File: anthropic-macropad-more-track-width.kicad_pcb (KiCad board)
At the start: 2 copper layers, 136 x 81 mm, 14 parts, among them SW1 ESC, SW10 ENTER, SW11 MIC, SW2 TAB, SW3 ALLOW_ONCE, SW4 UP, SW5 ALLOW_ALWAYS, SW6 LEFT, SW7 DOWN, SW8 RIGHT, SW9 REJECT, U1 XIAO_RP2040

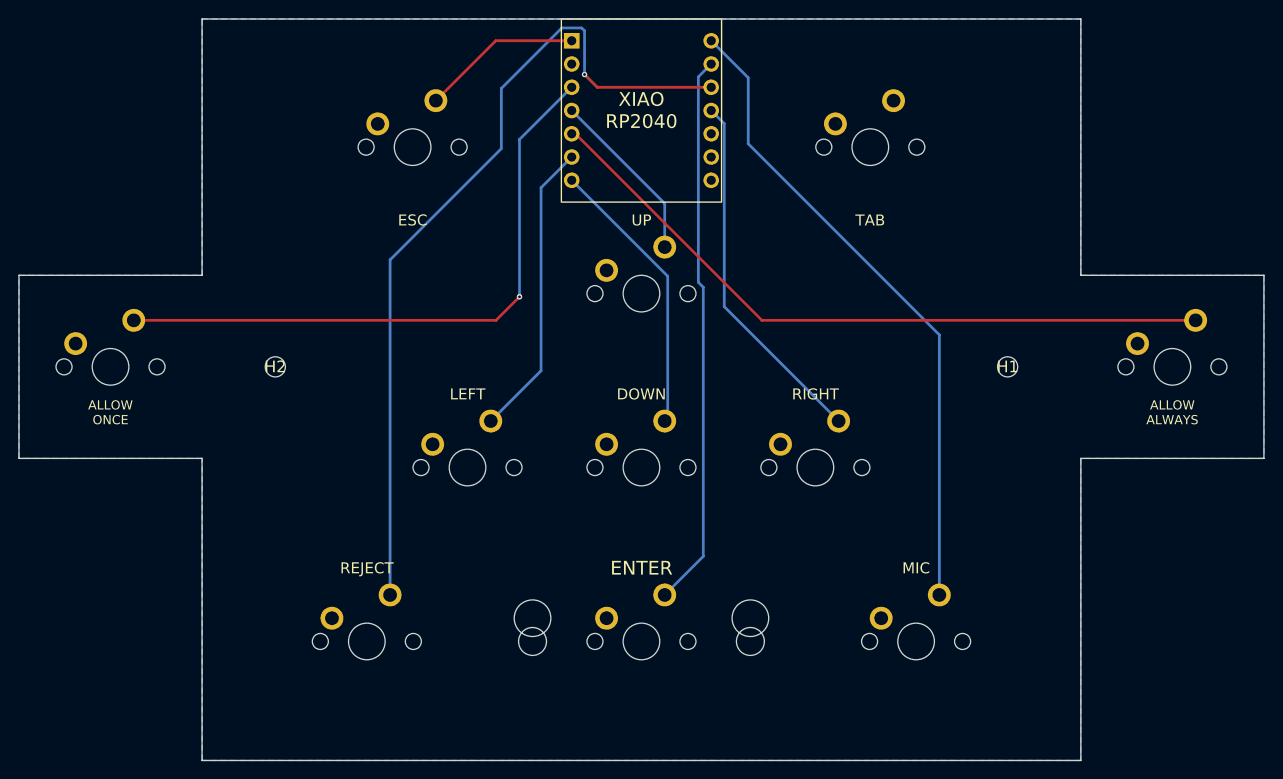
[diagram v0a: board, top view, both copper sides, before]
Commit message: Replace 2 mounting holes with 4 corner mounting holes
Co-Authored-By: Claude Opus 4.6 <noreply@anthropic.com>
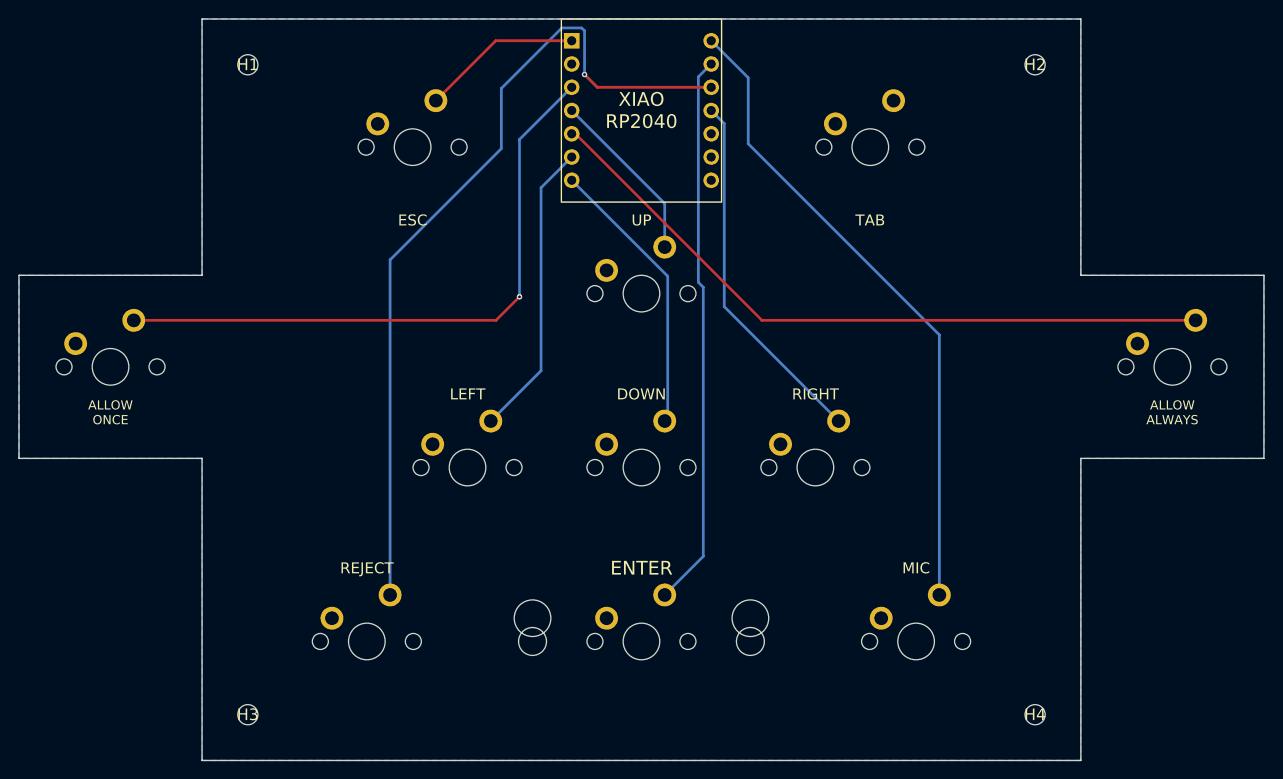
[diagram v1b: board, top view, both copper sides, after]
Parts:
- added H3: , MountingHole:MountingHole_2.2mm_M2, F.Cu at (57.0, 106.0)
- added H4: , MountingHole:MountingHole_2.2mm_M2, F.Cu at (143.0, 106.0)
- moved H1 89.3 mm to (57.0, 35.0)
- moved H2 89.3 mm to (143.0, 35.0)
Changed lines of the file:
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@@
 	(footprint "MountingHole:MountingHole_2.2mm_M2"
 		(layer "F.Cu")
-		(at 140 68)
+		(at 57 35)
 		(descr "Mounting Hole 2.2mm M2")
 		(property "Reference" "H1"
@@
 		(embedded_fonts no)
 	)
+	(footprint "MountingHole:MountingHole_2.2mm_M2"
+		(layer "F.Cu")
+		(at 143 106)
+		(descr "Mounting Hole 2.2mm M2")
+		(property "Reference" "H4"
+			(at 0 0 0)
+			(layer "F.SilkS")
+			(effects
+				(font
+					(size 1.27 1.27)
+				)
+			)
+		)
+		(property "Value" ""
+			(at 0 0 0)
+			(layer "F.Fab")
+			(effects
+				(font
+					(size 1.27 1.27)
+				)
+			)
+		)
+		(property "Datasheet" ""
+			(at 0 0 0)
+			(layer "F.Fab")
+			(hide yes)
+			(effects
+				(font
+					(size 1.27 1.27)
+				)
+			)
+		)
+		(property "Description" ""
+			(at 0 0 0)
+			(layer "F.Fab")
+			(hide yes)
+			(effects
+				(font
+					(size 1.27 1.27)
+				)
+			)
+		)
+		(attr exclude_from_pos_files exclude_from_bom)
+		(duplicate_pad_numbers_are_jumpers no)
+		(pad "" np_thru_hole circle
+			(at 0 0)
+			(size 2.2 2.2)
+			(drill 2.2)
+			(layers "*.Cu" "*.Mask")
+		)
+		(embedded_fonts no)
+	)
 	(footprint "Switch:SW_Cherry_MX_1u"
 		(layer "F.Cu")
@@
 	(footprint "MountingHole:MountingHole_2.2mm_M2"
 		(layer "F.Cu")
-		(at 60 68)
+		(at 143 35)
 		(descr "Mounting Hole 2.2mm M2")
 		(property "Reference" "H2"
@@
 		)
 		(embedded_fonts no)
+	)
+	(footprint "MountingHole:MountingHole_2.2mm_M2"
+		(layer "F.Cu")
+		(at 57 106)
+		(descr "Mounting Hole 2.2mm M2")
+		(property "Reference" "H3"
+			(at 0 0 0)
+			(layer "F.SilkS")
+			(effects
+				(font
+					(size 1.27 1.27)
+				)
+			)
+		)
+		(property "Value" ""
+			(at 0 0 0)
+			(layer "F.Fab")
+			(effects
+				(font
+					(size 1.27 1.27)
+				)
+			)
+		)
+		(property "Datasheet" ""
+			(at 0 0 0)
+			(layer "F.Fab")
+			(hide yes)
+			(effects
+				(font
+					(size 1.27 1.27)
+				)
+			)
+		)
+		(property "Description" ""
+			(at 0 0 0)
+			(layer "F.Fab")
+			(hide yes)
+			(effects
+				(font
+					(size 1.27 1.27)
+				)
+			)
+		)
+		(attr exclude_from_pos_files exclude_from_bom)
+		(duplicate_pad_numbers_are_jumpers no)
+		(pad "" np_thru_hole circle
+			(at 0 0)
+			(size 2.2 2.2)
+			(drill 2.2)
+			(layers "*.Cu" "*.Mask")
+		)
+		(embedded_fonts no)

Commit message: Fix GND pour connection and SW_TAB trace, DRC clean
Co-Authored-By: Claude Opus 4.6 <noreply@anthropic.com>
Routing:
- net SW_TAB: track 0.00 -> 67.9 mm
- net SW_ENTER: track 60.6 -> 85.5 mm
- net SW_MIC: track 70.9 -> 81.6 mm
- net SW_REJECT: track 91.5 -> 87.3 mm, vias 1 -> 0
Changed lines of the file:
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@@
 	)
 	(segment
-		(start 109.0415 41.4215)
+		(start 121.54 73.92)
+		(end 121.54 67.04)
+		(width 0.3)
+		(layer "B.Cu")
+		(net "SW_RIGHT")
+	)
+	(segment
+		(start 112 57.5)
+		(end 112 44.38)
+		(width 0.3)
+		(layer "B.Cu")
+		(net "SW_RIGHT")
+	)
+	(segment
+		(start 112 44.38)
 		(end 107.62 40)
 		(width 0.3)
@@
 	)
 	(segment
-		(start 109.0415 61.4215)
-		(end 109.0415 41.4215)
+		(start 121.54 67.04)
+		(end 112 57.5)
 		(width 0.3)
 		(layer "B.Cu")
@@
 	)
 	(segment
-		(start 121.54 73.92)
-		(end 109.0415 61.4215)
-		(width 0.3)
-		(layer "B.Cu")
-		(net "SW_RIGHT")
+		(start 92.38 34.92)
+		(end 102.5 45.04)
+		(width 0.3)
+		(layer "F.Cu")
+		(net "SW_TAB")
+	)
+	(segment
+		(start 102.5 48.5)
+		(end 108.5 54.5)
+		(width 0.3)
+		(layer "F.Cu")
+		(net "SW_TAB")
+	)
+	(segment
+		(start 129.42 38.92)
+		(end 127.54 38.92)
+		(width 0.3)
+		(layer "F.Cu")
+		(net "SW_TAB")
+	)
+	(segment
+		(start 108.5 54.5)
+		(end 128.5 54.5)
+		(width 0.3)
+		(layer "F.Cu")
+		(net "SW_TAB")
+	)
+	(segment
+		(start 128.5 54.5)
+		(end 134 49)
+		(width 0.3)
+		(layer "F.Cu")
+		(net "SW_TAB")
+	)
+	(segment
+		(start 134 49)
+		(end 134 43.5)
+		(width 0.3)
+		(layer "F.Cu")
+		(net "SW_TAB")
+	)
+	(segment
+		(start 102.5 45.04)
+		(end 102.5 48.5)
+		(width 0.3)
+		(layer "F.Cu")
+		(net "SW_TAB")
+	)
+	(segment
+		(start 134 43.5)
+		(end 129.42 38.92)
+		(width 0.3)
+		(layer "F.Cu")
+		(net "SW_TAB")
 	)
 	(segment
@@
 	)
 	(segment
-		(start 111.658 36.418)
+		(start 132.54 92.92)
+		(end 132.54 39.04)
+		(width 0.3)
+		(layer "B.Cu")
+		(net "SW_MIC")
+	)
+	(segment
+		(start 132.54 39.04)
+		(end 125.88 32.38)
+		(width 0.3)
+		(layer "B.Cu")
+		(net "SW_MIC")
+	)
+	(segment
+		(start 125.88 32.38)
 		(end 107.62 32.38)
 		(width 0.3)
@@
 	)
 	(segment
-		(start 111.658 43.63)
-		(end 111.658 36.418)
-		(width 0.3)
-		(layer "B.Cu")
-		(net "SW_MIC")
-	)
-	(segment
-		(start 132.54 64.512)
-		(end 111.658 43.63)
-		(width 0.3)
-		(layer "B.Cu")
-		(net "SW_MIC")
-	)
-	(segment
-		(start 132.54 92.92)
-		(end 132.54 64.512)
-		(width 0.3)
-		(layer "B.Cu")
-		(net "SW_MIC")
-	)
-	(segment
-		(start 106.7567 59.3055)
-		(end 106.7567 88.7033)
-		(width 0.3)
-		(layer "B.Cu")
-		(net "SW_ENTER")
-	)
-	(segment
-		(start 106.7567 88.7033)
-		(end 102.54 92.92)
-		(width 0.3)
-		(layer "B.Cu")
-		(net "SW_ENTER")
-	)
-	(segment
-		(start 106.2183 58.7671)
-		(end 106.7567 59.3055)
-		(width 0.3)
-		(layer "B.Cu")
-		(net "SW_ENTER")
-	)
-	(segment
-		(start 107.62 34.92)
-		(end 106.2183 36.3217)
-		(width 0.3)
-		(layer "B.Cu")
-		(net "SW_ENTER")
-	)
-	(segment
-		(start 106.2183 36.3217)
-		(end 106.2183 58.7671)
-		(width 0.3)
-		(layer "B.Cu")
-		(net "SW_ENTER")
-	)
-	(segment
-		(start 93.7817 36.0628)
-		(end 95.1789 37.46)
-		(width 0.3)
-		(layer "F.Cu")
-		(net "SW_REJECT")
-	)
-	(segment
-		(start 95.1789 37.46)
-		(end 107.62 37.46)
-		(width 0.3)
-		(layer "F.Cu")
-		(net "SW_REJECT")
-	)
-	(via
-		(at 93.7817 36.0628)
-		(size 0.6)
-		(drill 0.3)
-		(layers "F.Cu" "B.Cu")
-		(net "SW_REJECT")
-	)
-	(segment
-		(start 93.7817 31.291)
-		(end 93.7817 36.0628)
-		(width 0.3)
-		(layer "B.Cu")
-		(net "SW_REJECT")
-	)
-	(segment
-		(start 91.3015 30.9783)
-		(end 93.469 30.9783)
-		(width 0.3)
-		(layer "B.Cu")
-		(net "SW_REJECT")
-	)
-	(segment
-		(start 84.6925 44.1572)
-		(end 84.6925 37.5873)
-		(width 0.3)
-		(layer "B.Cu")
-		(net "SW_REJECT")
-	)
-	(segment
-		(start 72.54 56.3097)
-		(end 84.6925 44.1572)
-		(width 0.3)
-		(layer "B.Cu")
-		(net "SW_REJECT")
-	)
-	(segment
-		(start 93.469 30.9783)
-		(end 93.7817 31.291)
-		(width 0.3)
-		(layer "B.Cu")
-		(net "SW_REJECT")
-	)
-	(segment
-		(start 72.54 92.92)
-		(end 72.54 56.3097)
-		(width 0.3)
-		(layer "B.Cu")
-		(net "SW_REJECT")
-	)
-	(segment
-		(start 84.6925 37.5873)
-		(end 91.3015 30.9783)
-		(width 0.3)
-		(layer "B.Cu")
+		(start 109.46 86)
+		(end 122.5 86)
+		(width 0.3)
+		(layer "B.Cu")
+		(net "SW_ENTER")
+	)
+	(segment
+		(start 115 53.5)
+		(end 115 42.3)
+		(width 0.3)
+		(layer "B.Cu")
+		(net "SW_ENTER")
+	)
+	(segment
+		(start 129 67.5)
+		(end 115 53.5)
+		(width 0.3)
+		(layer "B.Cu")
+		(net "SW_ENTER")
+	)
+	(segment
+		(start 129 79.5)
+		(end 129 67.5)
+		(width 0.3)
+		(layer "B.Cu")
+		(net "SW_ENTER")
+	)
+	(segment
+		(start 122.5 86)
+		(end 129 79.5)
+		(width 0.3)
+		(layer "B.Cu")
+		(net "SW_ENTER")
+	)
+	(segment
+		(start 115 42.3)
+		(end 107.62 34.92)
+		(width 0.3)
+		(layer "B.Cu")
+		(net "SW_ENTER")
+	)
+	(segment
+		(start 102.54 92.92)
+		(end 109.46 86)
+		(width 0.3)
+		(layer "B.Cu")
+		(net "SW_ENTER")
+	)
+	(segment
+		(start 109 79.5)
+		(end 103 85.5)
+		(width 0.3)
+		(layer "B.Cu")
+		(net "SW_REJECT")
+	)
+	(segment
+		(start 107.62 37.46)
+		(end 107.96 37.46)
+		(width 0.3)
+		(layer "B.Cu")
+		(net "SW_REJECT")
+	)
+	(segment
+		(start 108 37.5)
+		(end 105 40.5)
+		(width 0.3)
+		(layer "B.Cu")
+		(net "SW_REJECT")
+	)
+	(segment
+		(start 105 51.5)
+		(end 109 55.5)
+		(width 0.3)
+		(layer "B.Cu")
+		(net "SW_REJECT")
+	)
+	(segment
+		(start 79.96 85.5)
+		(end 72.54 92.92)
+		(width 0.3)
+		(layer "B.Cu")
+		(net "SW_REJECT")
+	)
+	(segment
+		(start 107.96 37.46)
+		(end 108 37.5)
+		(width 0.3)
+		(layer "B.Cu")
+		(net "SW_REJECT")
+	)
+	(segment
+		(start 105 40.5)
+		(end 105 51.5)
+		(width 0.3)
+		(layer "B.Cu")
+		(net "SW_REJECT")
+	)
+	(segment
+		(start 109 55.5)
+		(end 109 79.5)
+		(width 0.3)
+		(layer "B.Cu")
+		(net "SW_REJECT")
+	)
+	(segment
+		(start 103 85.5)
+		(end 79.96 85.5)
+		(width 0.3)
+		(layer "B.Cu")

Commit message: Manual trace adjustments, DRC still clean
Co-Authored-By: Claude Opus 4.6 <noreply@anthropic.com>
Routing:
- net SW_ALLOW_ONCE: vias 1 -> 0
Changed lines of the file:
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@@
-	)
-	(segment
-		(start 44.54 62.92)
-		(end 84.1067 62.92)
-		(width 0.3)
-		(layer "F.Cu")
-		(net "SW_ALLOW_ONCE")
 	)
 	(segment
@@
 		(end 86.6767 60.35)
 		(width 0.3)
-		(layer "F.Cu")
-		(net "SW_ALLOW_ONCE")
-	)
-	(via
-		(at 86.6767 60.35)
-		(size 0.6)
-		(drill 0.3)
-		(layers "F.Cu" "B.Cu")
+		(layer "B.Cu")
 		(net "SW_ALLOW_ONCE")
 	)
@@
 		(width 0.3)
 		(layer "B.Cu")
+		(net "SW_ALLOW_ONCE")
+	)
+	(segment
+		(start 44.54 62.92)
+		(end 84.1067 62.92)
+		(width 0.3)
+		(layer "B.Cu")
